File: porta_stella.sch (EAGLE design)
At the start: 105 parts, among them CN4 MicroUSB, IC1 74LS00D, J1 PJ-393, T1 2N3904, T2 PN3906, T3 PN3906, T4 PN3906, T5 MMUN2133LT1G, U1 TPS61090RSAR, U2 MCP73871, X1 SSW-112-02-G-Q

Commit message: ready to finish wiring
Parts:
- removed GND_V: GND_V, wirepad:WIREPAD2,54/1,1
- removed S2: L_FIRE, SparkFun-Switches:MOMENTARY-SWITCH-SPST-SMD-5.2MM
- added GND_CVID: GND_CVID, wirepad:WIREPAD2,54/1,1
- added J2: SJ-43516-SMT, tiny_stella:SJ-43516-SMT
- added SW1: E-SWITCH_JS5208E-SWITCH_JS5208_0_0, tiny_stella:E-SWITCH_JS5208E-SWITCH_JS5208_0_0
- added U$7: TL3300DF260Q, tiny_stella:TL3300DF260Q
- J1: value PJ-393 -> 2p-smd-1.0-90d; device Seeed-Connector:AUDIO-JACK-PJ-393(8P-SMD) -> Seeed-Connector:SMD-JST-2P-1.0-90D
- U$5: value JS5208 -> 3352P-1-103LF; device tiny_stella:JS5208 -> tiny_stella:3352P-1-103LF
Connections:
- net N$8 renamed RAW_CVID
- new net AUD: J2.RING1, J2.TIP, U$5.A
- new net CVID: J2.SLEEVE
- new net JACK_AUD_OUT_L: J2.TIP_SWITCH
- new net JACK_AUD_OUT_R: J2.RING_SWITCH
- new net N$56: SW1.4
- new net N$8: AUD.P
- net GND: now also GND_CVID.P, J1.2, J2.RING2, SW1.PUSH(N.O.), U$5.E, U$7.P$3, U$7.P$4; no longer GND_V.P, S2.2, U$5.GND
- net LFT_FIRE: now also U$7.P$1, U$7.P$2; no longer S2.1
- net LFT_JOY_DWN: now also SW1.2; no longer U$5.C-D
- net LFT_JOY_LFT: now also SW1.6; no longer U$5.B-L
- net LFT_JOY_RGT: now also SW1.5; no longer U$5.D-R
- net LFT_JOY_UP: now also SW1.COMM.; no longer U$5.A-U
- net N$28: now also U$5.S; no longer AUD.P
- net VLIPO: now also J1.1
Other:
- note added: "Atari 2600"
- note added: "Battery and Power Circuitry Referenced from the Powerboost 1000 By Adafruit"
- note added: "Composite Video Amplifier By Simon Plata"
- note added: "Pause Switch Circuitry By Victor Trucco www.victortrucco.com"
- moved on the sheet: AUD, BRIGHT, C1, C10, C11, C14, C15, C16, C17, C18, C19, C2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

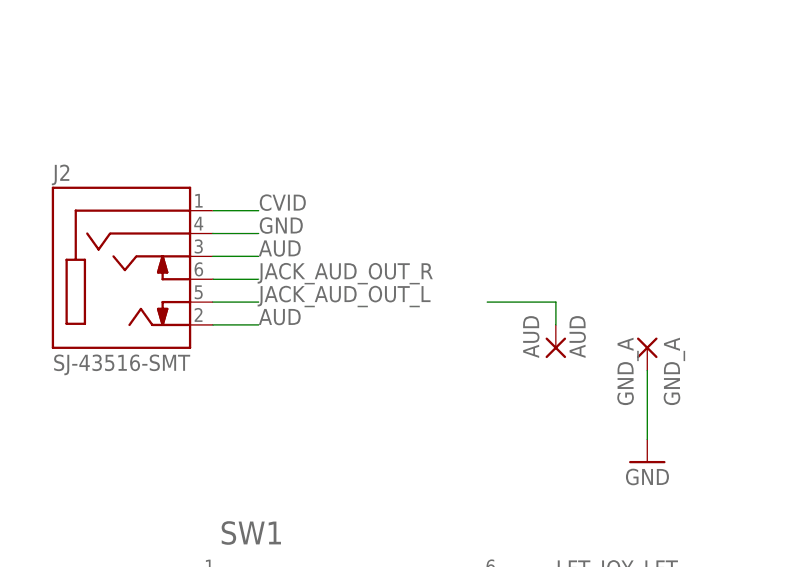
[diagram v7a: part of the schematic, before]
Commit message: Finished traces, just need to label components:
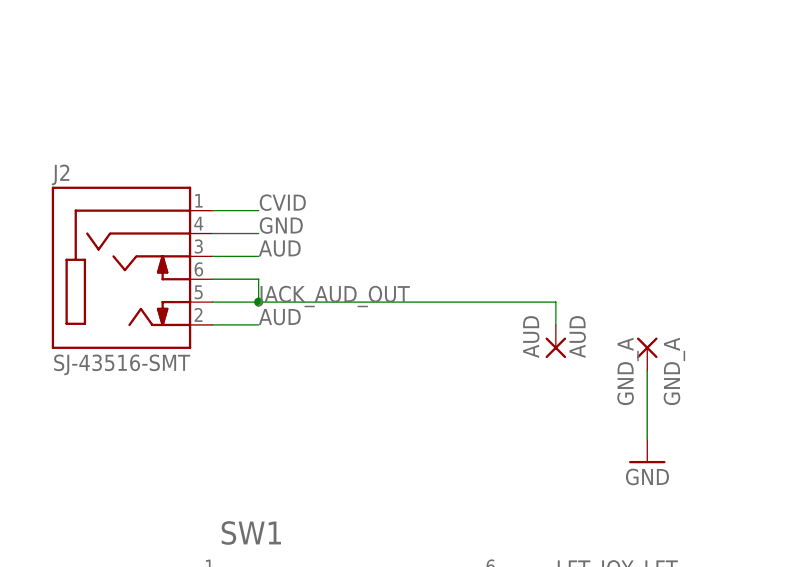
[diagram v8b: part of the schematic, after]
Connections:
- removed net JACK_AUD_OUT_L: J2.TIP_SWITCH
- removed net JACK_AUD_OUT_R: J2.RING_SWITCH
- removed net N$25: CVID.P, R25.1, T2.C
- removed net N$8: AUD.P
- new net JACK_AUD_OUT: AUD.P, J2.RING_SWITCH, J2.TIP_SWITCH
- net CVID: now also CVID.P, R25.1, T2.C
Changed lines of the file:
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@@
-</segment>
-</net>
-<net name="N$25" class="0">
-<segment>
-<pinref part="T2" gate="G$1" pin="C"/>
-<pinref part="R25" gate="G$1" pin="1"/>
-<wire x1="269.24" y1="-22.86" x2="269.24" y2="-25.4" width="0.1524" layer="91"/>
-<wire x1="269.24" y1="-25.4" x2="276.86" y2="-25.4" width="0.1524" layer="91"/>
-<junction x="269.24" y="-25.4"/>
-<pinref part="CVID" gate="G$1" pin="P"/>
 </segment>
 </net>
@@
 <label x="241.3" y="114.3" size="1.778" layer="95"/>
 </segment>
+<segment>
+<pinref part="T2" gate="G$1" pin="C"/>
+<pinref part="R25" gate="G$1" pin="1"/>
+<wire x1="269.24" y1="-22.86" x2="269.24" y2="-25.4" width="0.1524" layer="91"/>
+<wire x1="269.24" y1="-25.4" x2="276.86" y2="-25.4" width="0.1524" layer="91"/>
+<junction x="269.24" y="-25.4"/>
+<pinref part="CVID" gate="G$1" pin="P"/>
+</segment>
 </net>
 <net name="AUD" class="0">
@@
 </segment>
 </net>
-<net name="JACK_AUD_OUT_R" class="0">
+<net name="JACK_AUD_OUT" class="0">
 <segment>
 <pinref part="J2" gate="G$1" pin="RING_SWITCH"/>
 <wire x1="236.22" y1="106.68" x2="241.3" y2="106.68" width="0.1524" layer="91"/>
-<label x="241.3" y="106.68" size="1.778" layer="95"/>
-</segment>
-</net>
-<net name="JACK_AUD_OUT_L" class="0">
-<segment>
 <pinref part="J2" gate="G$1" pin="TIP_SWITCH"/>
-<wire x1="236.22" y1="104.14" x2="241.3" y2="104.14" width="0.1524" layer="91"/>
 <label x="241.3" y="104.14" size="1.778" layer="95"/>
-</segment>
-</net>
-<net name="N$8" class="0">
-<segment>
 <pinref part="AUD" gate="G$1" pin="P"/>
 <wire x1="274.32" y1="101.6" x2="274.32" y2="104.14" width="0.1524" layer="91"/>
-<wire x1="274.32" y1="104.14" x2="266.7" y2="104.14" width="0.1524" layer="91"/>
-</segment>
-</net>
+<wire x1="236.22" y1="104.14" x2="241.3" y2="104.14" width="0.1524" layer="91"/>
+<wire x1="241.3" y1="104.14" x2="274.32" y2="104.14" width="0.1524" layer="91"/>
+<wire x1="241.3" y1="106.68" x2="241.3" y2="104.14" width="0.1524" layer="91"/>
+<junction x="241.3" y="104.14"/>
+</segment>
+</net>
